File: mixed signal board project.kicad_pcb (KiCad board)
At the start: 4 copper layers, 70.4 x 72.2 mm, 189 parts, among them J101 USB_B_Mini, J102 Conn_01x06_Pin, J201 8P8C_Shielded, J301 Conn_01x04_Pin, J401 AudioJack2_Ground, J402 Conn_01x04_Pin, J403 Screw_Terminal_01x03, J501 USB_B_Mini, J701 Conn_01x02_Socket, J801 Conn_01x02_Socket, J901 UART_CONN, J902 CAN_CONN, SW101 SW_SPDT, SW201 SW_SPDT, SW901 SW_SPDT, U101 STM32F103C8Tx, U11 LD1117S33TR_SOT223, U12 LD1117S18TR_SOT223, U201 DP83826ERHBR, U301 ADS122C04IPW, U401 CS43L22-CNZ, U402 IMP34DT05TR, U501 CH340C, U701 DMHT6016LFJ-13, U702 DRV8701, U801 DMHT6016LFJ-13, U802 DRV8701, U901 STM32F407VGTx, Y201 25Mhz, Y901 8MHz

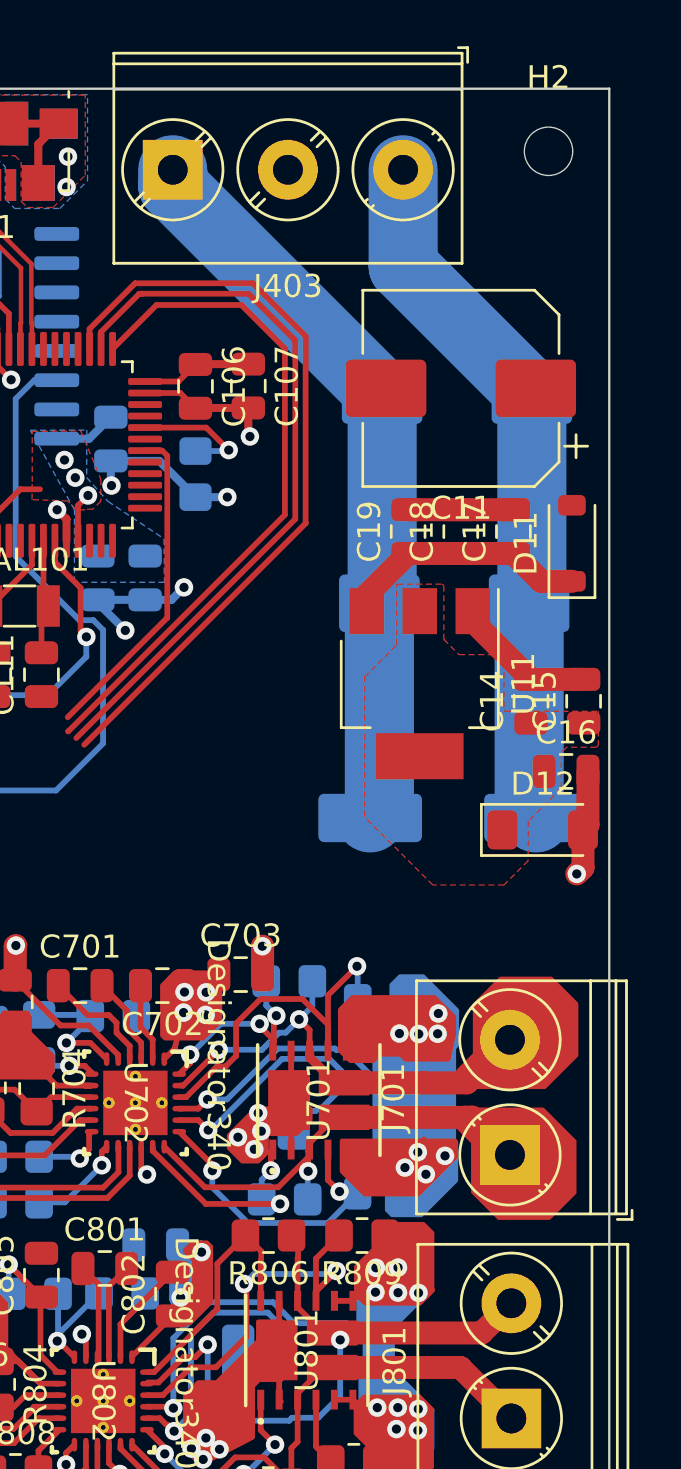
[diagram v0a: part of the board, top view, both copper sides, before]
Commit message: some changes on experimente branch, layout, 12v and gnd tracks of power jack deleted.
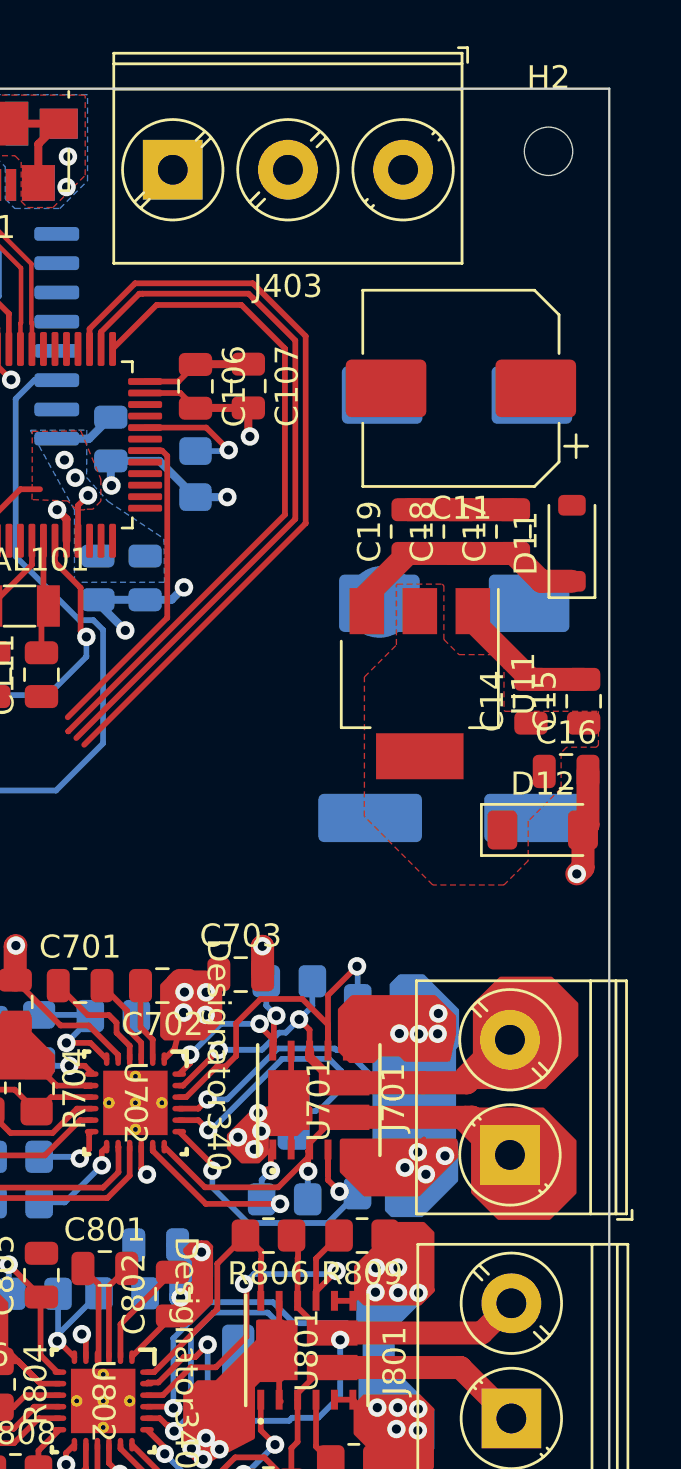
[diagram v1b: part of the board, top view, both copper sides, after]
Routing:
- net GND: track 220.2 -> 188.3 mm
- net +12V: track 59.0 -> 28.3 mm

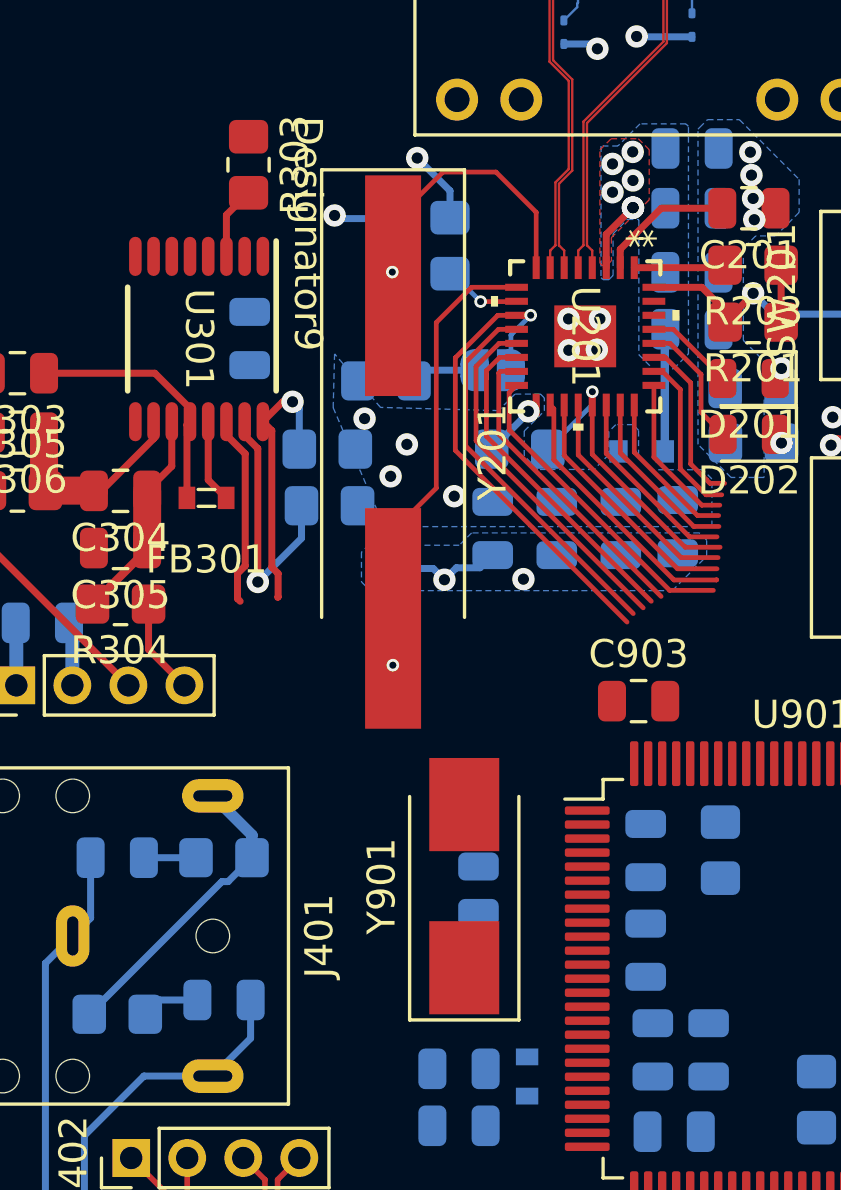
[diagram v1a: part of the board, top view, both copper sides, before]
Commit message: layout re-design start
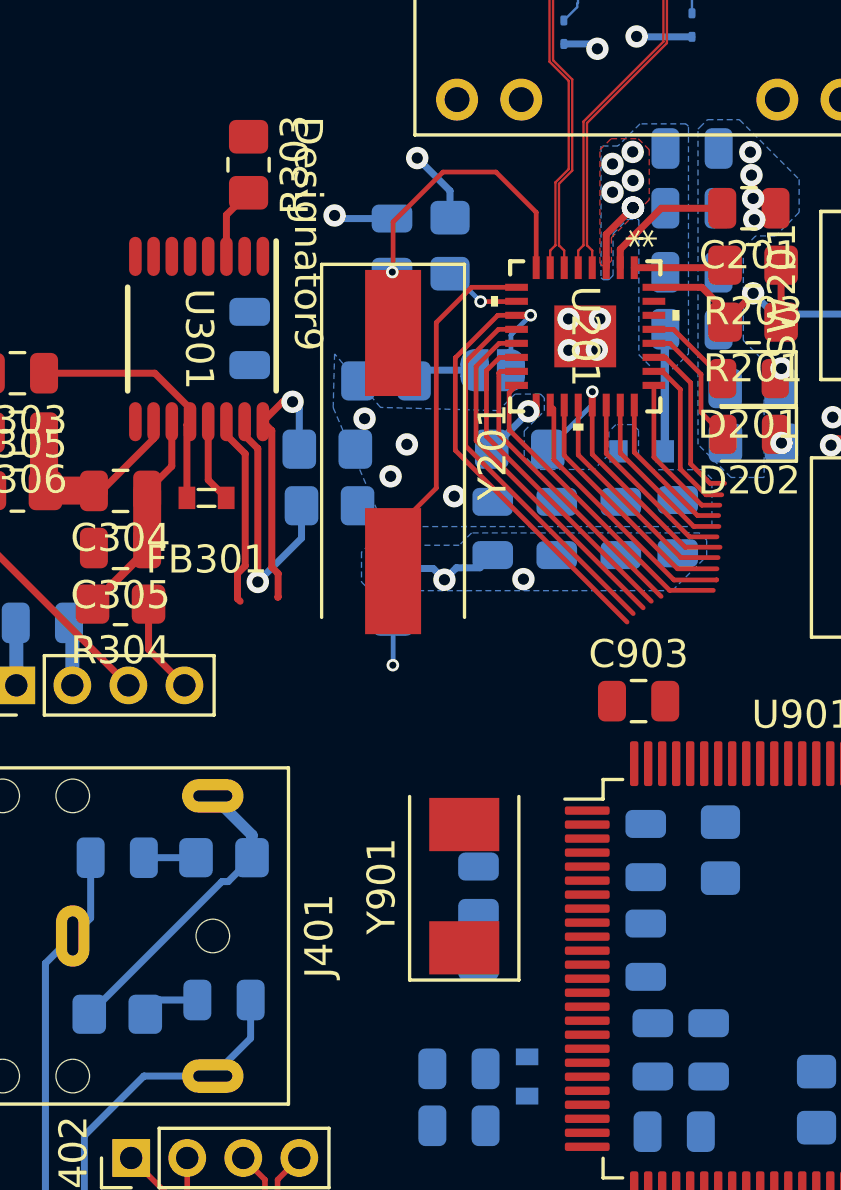
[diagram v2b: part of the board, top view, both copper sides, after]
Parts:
- Y201: footprint Crystal:Crystal_SMD_HC49-SD_HandSoldering -> Crystal:Crystal_SMD_HC49-SD
- Y901: footprint Crystal:Crystal_SMD_0603-2Pin_6.0x3.5mm_HandSoldering -> Crystal:Crystal_SMD_0603-2Pin_6.0x3.5mm

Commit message: ethernet, debugger and usb layouts re-designed
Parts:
- C106, R102: moved to B.Cu
- C12, C13, C20, C202, C203, C204, C205, C206, C207, C21, C22, C301, C302, C401, C402, C403, C404, C405, C410, C413, C414, C415, C416, C417, C704, C705, C803, C901, C902, C904, C906, C907, C908, C909, C910, C911, C912, C913, C914, C915, C916, C917, D13, D14, FB201, FB401, FB901, R202, R204, R205, R206, R207, R208, R301, R302, R402, R403, R701, R702, R703, R706, R707, R708, R709, R710, R711, R801, R802, R810, R811, R901, R902, R903, U12: moved to F.Cu
- H1, H2, H3, H4: footprint MountingHole:MountingHole_2.1mm -> MountingHole:MountingHole_2.2mm_M2_ISO7380_Pad
- J401: value AudioJack2_Ground -> AudioJack3; footprint Connector_Audio:Jack_3.5mm_CUI_SJ1-3523N_Horizontal -> Connector_Audio:Jack_3.5mm_CUI_SJ-3523-SMT_Horizontal
- SW101, SW201: footprint footprints:SW_PTS636_SM43J_SMTR_LFS -> Button_Switch_SMD:SW_SPST_B3U-1000P
- SW901: footprint Button_Switch_SMD:SW_Tactile_SPST_NO_Straight_CK_PTS636Sx25SMTRLFS -> Button_Switch_SMD:SW_SPST_B3U-1000P
- moved C913 162.1 mm to (255.6, 48.9), turned to 0 degrees
- moved C901 156.1 mm to (246.7, 48.9), turned to 0 degrees
- moved C902 155.7 mm to (246.7, 51.9), turned to 0 degrees
- moved C912 152.6 mm to (251.1, 64.0), turned to 0 degrees
- moved C911 152.5 mm to (251.1, 61.0), turned to 0 degrees
- moved C908 152.4 mm to (251.1, 51.9), turned to 0 degrees
- moved C914 151.9 mm to (255.6, 51.9), turned to 0 degrees
- moved C907 151.7 mm to (251.1, 48.9), turned to 0 degrees
- moved C909 151.7 mm to (251.1, 54.9), turned to 0 degrees
- moved J902 151.1 mm to (250.5, 67.5), turned to 0 degrees
- moved C705 150.6 mm to (277.7, 97.9), turned to 0 degrees
- moved C706 149.6 mm to (277.7, 100.9), turned to 0 degrees
- moved C916 147.4 mm to (255.6, 58.0), turned to 0 degrees
- moved R901 147.3 mm to (254.9, 67.0), turned to 0 degrees
- moved C701 146.9 mm to (277.7, 88.9)
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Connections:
- J401 pad S: Net-(U401-HP/LINE_OUTB) -> GND
- J401 pad T: Net-(U401-HP/LINE_OUTA) -> Net-(U401-HP/LINE_OUTB)
- JP201 pad 2: /Ethernet/ETH_MDIO -> +3V3
- R208 pad 1: +3V3 -> Net-(JP201-A)
- R208 pad 2: Net-(JP201-A) -> /Ethernet/ETH_MDIO
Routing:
- net GND: track 188.3 -> 0.00 mm, vias 46 -> 0
- net +3V3: track 64.4 -> 0.00 mm, vias 18 -> 0
- net /Debugger/JTMS_F407: track 63.3 -> 0.00 mm
- net /Ethernet/RJ_45_SH: track 41.3 -> 0.00 mm
- net /Debugger/JTCLK_F407: track 31.9 -> 0.00 mm
- net /STM32F407/CH340_~{RST}: track 31.4 -> 0.00 mm, vias 1 -> 0
- net /Motor_Driver2/SP_2: track 29.1 -> 0.00 mm, vias 9 -> 0
- net +12V: track 28.3 -> 0.00 mm, vias 18 -> 0
- net /Motor_Driver1/SH2: track 28.3 -> 0.00 mm, vias 2 -> 0
- net /STM32F407/CH340_RXD: track 25.0 -> 0.00 mm, vias 1 -> 0
- net Net-(U401-HP/LINE_OUTA): track 24.5 -> 0.00 mm, vias 1 -> 0
- net /Motor_Driver1/SP: track 24.3 -> 0.00 mm, vias 11 -> 0
- net Net-(U401-HP/LINE_OUTB): track 24.2 -> 0.00 mm, vias 1 -> 0
- net /STM32F407/CH340_TXD: track 23.7 -> 0.00 mm, vias 1 -> 0
- net /Motor_Driver1/SH1: track 23.3 -> 0.00 mm
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- removed copper zone on In2.Cu, net +12V
- removed copper zone on B.Cu, net +3.3VA
- removed copper zone on F.Cu, net +3.3VA
- removed copper zone on B.Cu, net +3V3
- removed copper zone on F.Cu, net +3V3
- removed copper zone on In2.Cu, net +3V3
- removed copper zone on B.Cu, net GND
- removed copper zone on F.Cu, net GND
- removed copper zone on In1.Cu, net GND
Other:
- board size 70.4 x 72.2 mm -> 70 x 70 mm

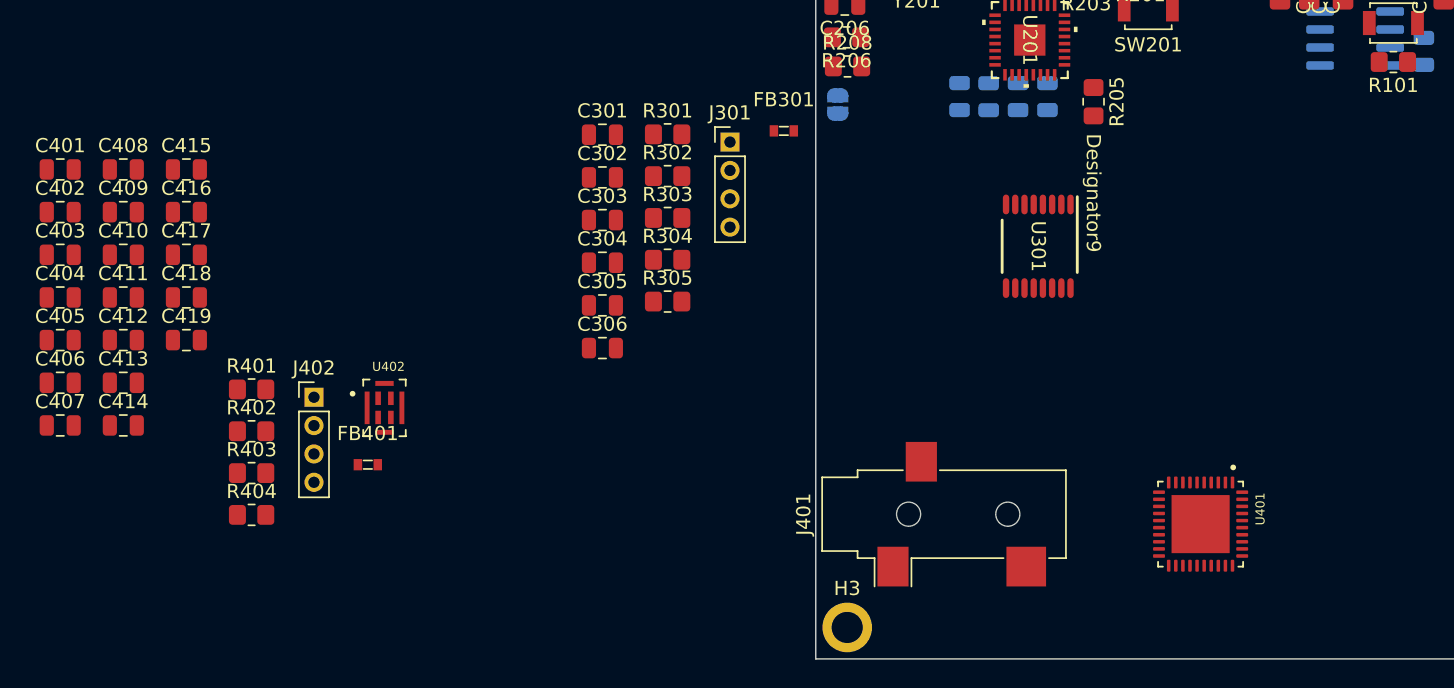
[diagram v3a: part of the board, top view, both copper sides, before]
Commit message: adc, dac and mi layouts re-designing...
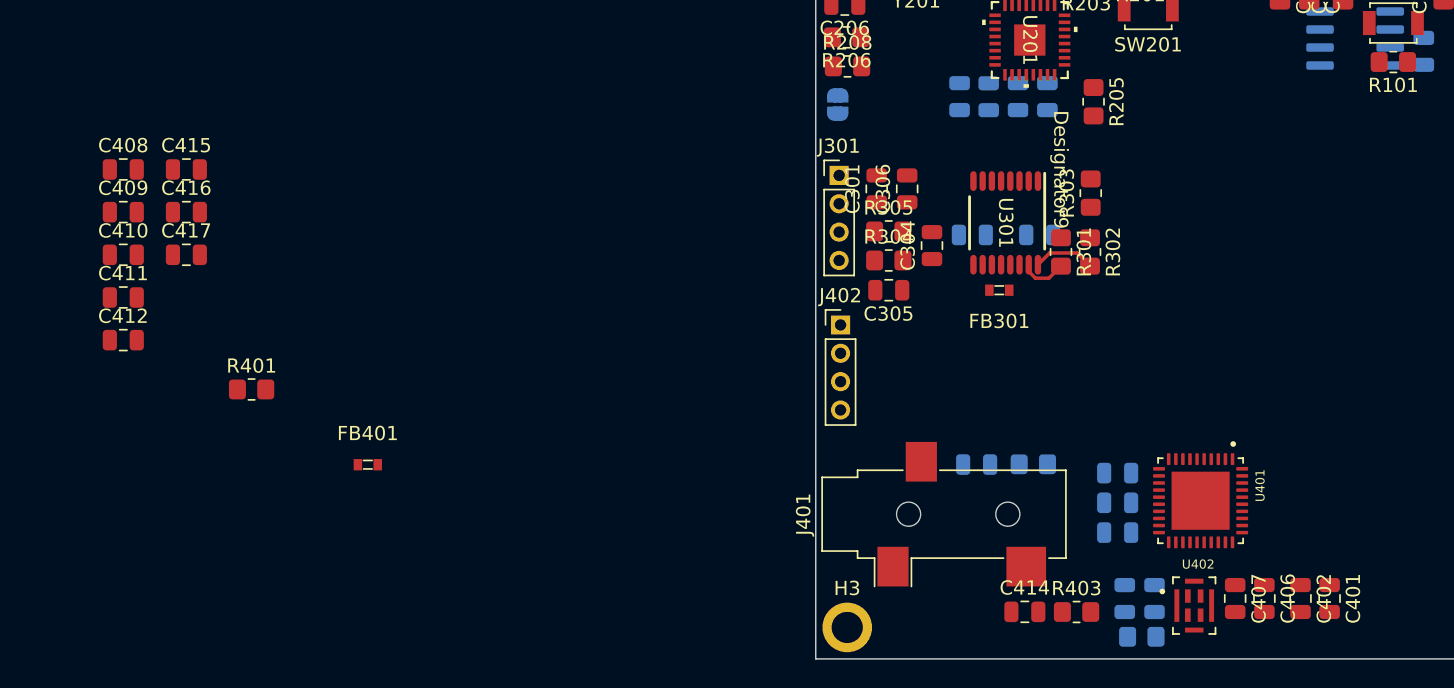
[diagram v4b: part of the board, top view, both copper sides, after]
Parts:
- C302, C303, C403, C404, C405, C413, C418, C419, R402, R404: moved to B.Cu
- moved C401 94.5 mm to (106.3, 119.2), turned to -90 degrees
- moved C402 91.6 mm to (104.2, 119.2), turned to -90 degrees
- moved C406 86.3 mm to (101.7, 119.2), turned to -90 degrees
- moved C407 83.8 mm to (99.6, 119.2), turned to -90 degrees
- moved C403 76.2 mm to (91.3, 110.3), turned to 180 degrees
- moved C404 76.0 mm to (91.3, 112.5), turned to 180 degrees
- moved C405 75.8 mm to (91.3, 114.5), turned to 180 degrees
- moved C418 71.5 mm to (94.0, 119.2), turned to -90 degrees
- moved C419 68.7 mm to (91.8, 119.2), turned to -90 degrees
- moved C414 64.9 mm to (84.8, 120.1)
- moved R404 63.4 mm to (93.0, 121.9), turned to 180 degrees
- moved C413 60.5 mm to (81.4, 109.8)
- moved R403 59.0 mm to (88.5, 120.2)
- moved U402 58.8 mm to (96.8, 119.7)
- moved R402 55.2 mm to (85.4, 109.7)
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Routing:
- net /ADC/SCK_ADC: track 0.00 -> 4.40 mm
- net /ADC/SDA_ADC: track 0.00 -> 3.30 mm

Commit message: all layouts re-designed.Next step routing...
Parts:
- removed C704: 100u, Capacitor_SMD:C_Elec_8x10.2
- C14, C15, C16, C17, C18, C19, C20, C21, C22, C23, C24, C25, C408, C409, C411, C415, C417, C701, C702, C703, C706, C803, C901, C902, C904, C905, C906, C909, C911, C914, C917, D11, D12, D13, D14, FB401, FB901, R401, R703, R704, R705, R706, R707, R708, R709, R711, R801, R802, R803, R806, R807, R808, R809, R811, R901, U11, U12, U701, U801: moved to B.Cu
- C403, C404, C405: moved to F.Cu
- C804: footprint Capacitor_SMD:C_Elec_8x10.2 -> Capacitor_SMD:CP_Elec_8x10
- moved C913 173.4 mm to (88.0, 93.8), turned to -90 degrees
- moved C912 165.2 mm to (88.0, 90.3), turned to 90 degrees
- moved C901 162.6 mm to (91.2, 96.5), turned to 180 degrees
- moved C902 162.3 mm to (91.2, 98.6), turned to 180 degrees
- moved C706 159.6 mm to (120.8, 71.5), turned to -90 degrees
- moved C909 158.2 mm to (99.0, 98.3), turned to 180 degrees
- moved C702 156.2 mm to (123.8, 65.8)
- moved R901 155.8 mm to (100.8, 89.4), turned to -90 degrees
- moved C705 155.8 mm to (124.0, 72.5), turned to 180 degrees
- moved C701 155.4 mm to (123.8, 67.8), turned to 180 degrees
- moved C917 155.3 mm to (102.8, 89.4), turned to -90 degrees
- moved C914 155.3 mm to (115.0, 118.2), turned to -90 degrees
- moved R709 153.0 mm to (123.8, 61.9), turned to 90 degrees
- moved R903 152.8 mm to (105.0, 102.7)
- moved C916 152.6 mm to (110.0, 103.5), turned to -90 degrees
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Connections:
- J403 pad 1: +12V -> GND
- J403 pad 3: GND -> +12V
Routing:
- net /DAC adn MIC/MCLK_DAC: track 0.00 -> 3.46 mm
- net /DAC adn MIC/SCLK_DAC: track 0.00 -> 3.00 mm
- net /DAC adn MIC/SDIN_DAC: track 0.00 -> 2.38 mm
- net /DAC adn MIC/LRCK_DAC: track 0.00 -> 1.62 mm
